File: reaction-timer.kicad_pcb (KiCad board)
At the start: 2 copper layers, 48 x 80 mm, 38 parts, among them IC1 4026, IC2 4026, IC3 4026, IC5 NE555P, IC6 NE555P, IC7 NE555P

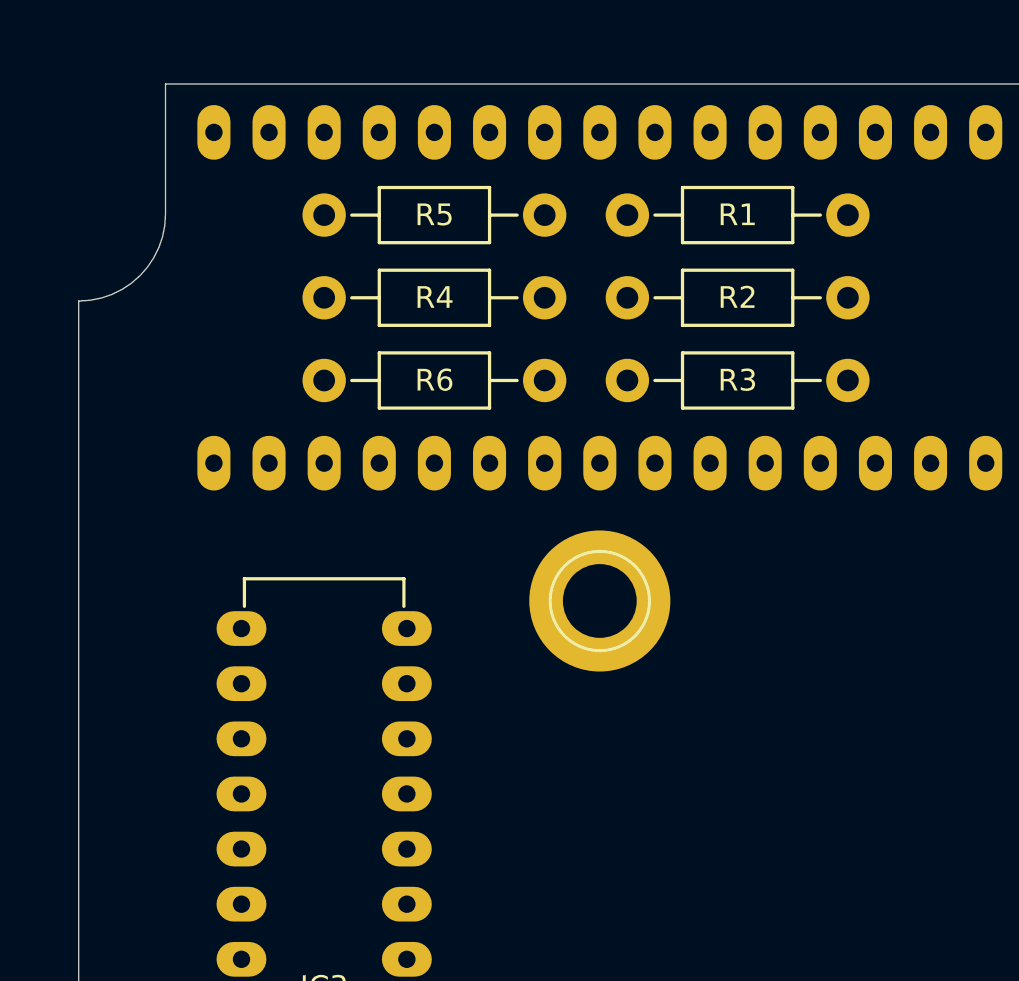
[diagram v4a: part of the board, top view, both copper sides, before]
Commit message: Start connecting some ICs on the PCB to see if it's feasible
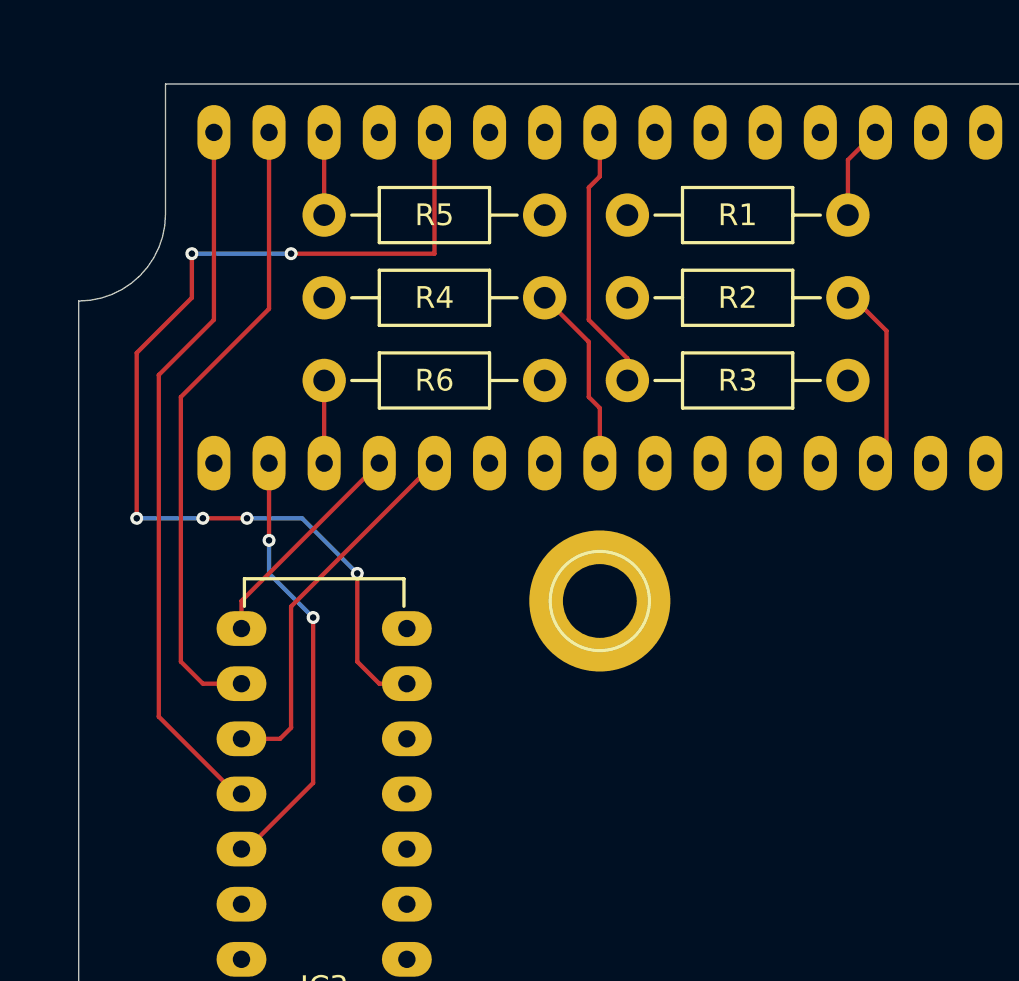
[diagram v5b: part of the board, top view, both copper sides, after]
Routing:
- net /G3: track 0.00 -> 48.0 mm, vias 0 -> 6
- net /B3: track 0.00 -> 33.3 mm
- net /A3: track 0.00 -> 29.3 mm
- net /C3: track 0.00 -> 20.1 mm, vias 0 -> 2
- net /E3: track 0.00 -> 17.4 mm
- net Net-(AFF2-Pad8): track 0.00 -> 12.4 mm
- net /D3: track 0.00 -> 10.3 mm
- net Net-(AFF1-Pad3): track 0.00 -> 8.72 mm
- net Net-(AFF2-Pad3): track 0.00 -> 8.67 mm
- net Net-(AFF1-Pad8): track 0.00 -> 4.34 mm
- net Net-(AFF3-Pad8): track 0.00 -> 3.81 mm
- net Net-(AFF3-Pad3): track 0.00 -> 3.81 mm
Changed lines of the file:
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@@
   (general
     (links 104)
-    (no_connects 104)
+    (no_connects 92)
     (area 17.504999 19.175 204.617501 195.285)
     (thickness 1.6)
     (drawings 8)
-    (tracks 0)
+    (tracks 60)
     (zones 0)
     (modules 38)
@@
   (gr_line (start 101.27 61.27) (end 101.27 67.27) (angle 90) (layer Edge.Cuts) (width 0.001))
   (gr_line (start 61.27 61.27) (end 101.27 61.27) (angle 90) (layer Edge.Cuts) (width 0.001))
+  (segment (start 92.71 71.12) (end 92.964 71.12) (width 0.2) (layer F.Cu) (net 3) (status C00000))
+  (segment (start 92.964 71.12) (end 94.488 72.644) (width 0.2) (layer F.Cu) (net 3) (status 400000))
+  (segment (start 94.488 72.644) (end 94.488 78.232) (width 0.2) (layer F.Cu) (net 3) (status 800000))
+  (segment (start 94.488 78.232) (end 93.98 78.74) (width 0.2) (layer F.Cu) (net 3) (status C00000))
+  (segment (start 92.71 67.31) (end 92.71 64.77) (width 0.2) (layer F.Cu) (net 8) (status 400000))
+  (segment (start 92.71 64.77) (end 93.98 63.5) (width 0.2) (layer F.Cu) (net 8) (status 800000))
+  (segment (start 81.28 78.74) (end 81.28 76.2) (width 0.2) (layer F.Cu) (net 13) (status 400000))
+  (segment (start 80.772 73.152) (end 78.74 71.12) (width 0.2) (layer F.Cu) (net 13) (status 800000))
+  (segment (start 80.772 75.692) (end 80.772 73.152) (width 0.2) (layer F.Cu) (net 13))
+  (segment (start 81.28 76.2) (end 80.772 75.692) (width 0.2) (layer F.Cu) (net 13))
+  (segment (start 81.28 63.5) (end 81.28 65.532) (width 0.2) (layer F.Cu) (net 18) (status 400000))
+  (segment (start 82.55 73.914) (end 82.55 74.93) (width 0.2) (layer F.Cu) (net 18) (status 800000))
+  (segment (start 80.772 72.136) (end 82.55 73.914) (width 0.2) (layer F.Cu) (net 18))
+  (segment (start 80.772 66.04) (end 80.772 72.136) (width 0.2) (layer F.Cu) (net 18))
+  (segment (start 81.28 65.532) (end 80.772 66.04) (width 0.2) (layer F.Cu) (net 18))
+  (segment (start 64.77 91.44) (end 66.548 91.44) (width 0.2) (layer F.Cu) (net 21) (status 400000))
+  (segment (start 67.056 85.344) (end 73.66 78.74) (width 0.2) (layer F.Cu) (net 21) (status 800000))
+  (segment (start 67.056 90.932) (end 67.056 85.344) (width 0.2) (layer F.Cu) (net 21))
+  (segment (start 66.548 91.44) (end 67.056 90.932) (width 0.2) (layer F.Cu) (net 21))
+  (segment (start 64.77 86.36) (end 64.77 85.09) (width 0.2) (layer F.Cu) (net 22) (status 400000))
+  (segment (start 64.77 85.09) (end 71.12 78.74) (width 0.2) (layer F.Cu) (net 22) (status 800000))
+  (segment (start 68.58 78.74) (end 68.58 74.93) (width 0.2) (layer F.Cu) (net 23) (status C00000))
+  (segment (start 64.77 96.52) (end 65.024 96.52) (width 0.2) (layer F.Cu) (net 24) (status C00000))
+  (segment (start 65.024 96.52) (end 68.072 93.472) (width 0.2) (layer F.Cu) (net 24) (status 400000))
+  (segment (start 68.072 93.472) (end 68.072 85.852) (width 0.2) (layer F.Cu) (net 24))
+  (via (at 68.072 85.852) (size 0.6) (layers F.Cu B.Cu) (net 24))
+  (segment (start 68.072 85.852) (end 66.04 83.82) (width 0.2) (layer B.Cu) (net 24))
+  (segment (start 66.04 83.82) (end 66.04 82.296) (width 0.2) (layer B.Cu) (net 24))
+  (via (at 66.04 82.296) (size 0.6) (layers F.Cu B.Cu) (net 24))
+  (segment (start 66.04 82.296) (end 66.04 78.74) (width 0.2) (layer F.Cu) (net 24) (status 800000))
+  (segment (start 64.77 93.98) (end 64.516 93.98) (width 0.2) (layer F.Cu) (net 26) (status C00000))
+  (segment (start 64.516 93.98) (end 60.96 90.424) (width 0.2) (layer F.Cu) (net 26) (status 400000))
+  (segment (start 60.96 90.424) (end 60.96 74.676) (width 0.2) (layer F.Cu) (net 26))
+  (segment (start 60.96 74.676) (end 63.5 72.136) (width 0.2) (layer F.Cu) (net 26))
+  (segment (start 63.5 72.136) (end 63.5 63.5) (width 0.2) (layer F.Cu) (net 26) (status 800000))
+  (segment (start 64.77 88.9) (end 62.992 88.9) (width 0.2) (layer F.Cu) (net 27) (status 400000))
+  (segment (start 66.04 71.628) (end 66.04 63.5) (width 0.2) (layer F.Cu) (net 27) (status 800000))
+  (segment (start 61.976 75.692) (end 66.04 71.628) (width 0.2) (layer F.Cu) (net 27))
+  (segment (start 61.976 87.884) (end 61.976 75.692) (width 0.2) (layer F.Cu) (net 27))
+  (segment (start 62.992 88.9) (end 61.976 87.884) (width 0.2) (layer F.Cu) (net 27))
+  (segment (start 68.58 67.31) (end 68.58 63.5) (width 0.2) (layer F.Cu) (net 28) (status C00000))
+  (segment (start 72.39 88.9) (end 71.12 88.9) (width 0.2) (layer F.Cu) (net 30) (status 400000))
+  (segment (start 73.66 69.088) (end 73.66 63.5) (width 0.2) (layer F.Cu) (net 30) (status 800000))
+  (segment (start 67.056 69.088) (end 73.66 69.088) (width 0.2) (layer F.Cu) (net 30))
+  (via (at 67.056 69.088) (size 0.6) (layers F.Cu B.Cu) (net 30))
+  (segment (start 62.484 69.088) (end 67.056 69.088) (width 0.2) (layer B.Cu) (net 30))
+  (via (at 62.484 69.088) (size 0.6) (layers F.Cu B.Cu) (net 30))
+  (segment (start 62.484 71.12) (end 62.484 69.088) (width 0.2) (layer F.Cu) (net 30))
+  (segment (start 59.944 73.66) (end 62.484 71.12) (width 0.2) (layer F.Cu) (net 30))
+  (segment (start 59.944 81.28) (end 59.944 73.66) (width 0.2) (layer F.Cu) (net 30))
+  (via (at 59.944 81.28) (size 0.6) (layers F.Cu B.Cu) (net 30))
+  (segment (start 62.992 81.28) (end 59.944 81.28) (width 0.2) (layer B.Cu) (net 30))
+  (via (at 62.992 81.28) (size 0.6) (layers F.Cu B.Cu) (net 30))
+  (segment (start 65.024 81.28) (end 62.992 81.28) (width 0.2) (layer F.Cu) (net 30))
+  (via (at 65.024 81.28) (size 0.6) (layers F.Cu B.Cu) (net 30))
+  (segment (start 67.564 81.28) (end 65.024 81.28) (width 0.2) (layer B.Cu) (net 30))
+  (segment (start 70.104 83.82) (end 67.564 81.28) (width 0.2) (layer B.Cu) (net 30))
+  (via (at 70.104 83.82) (size 0.6) (layers F.Cu B.Cu) (net 30))
+  (segment (start 70.104 87.884) (end 70.104 83.82) (width 0.2) (layer F.Cu) (net 30))
+  (segment (start 71.12 88.9) (end 70.104 87.884) (width 0.2) (layer F.Cu) (net 30))
 )

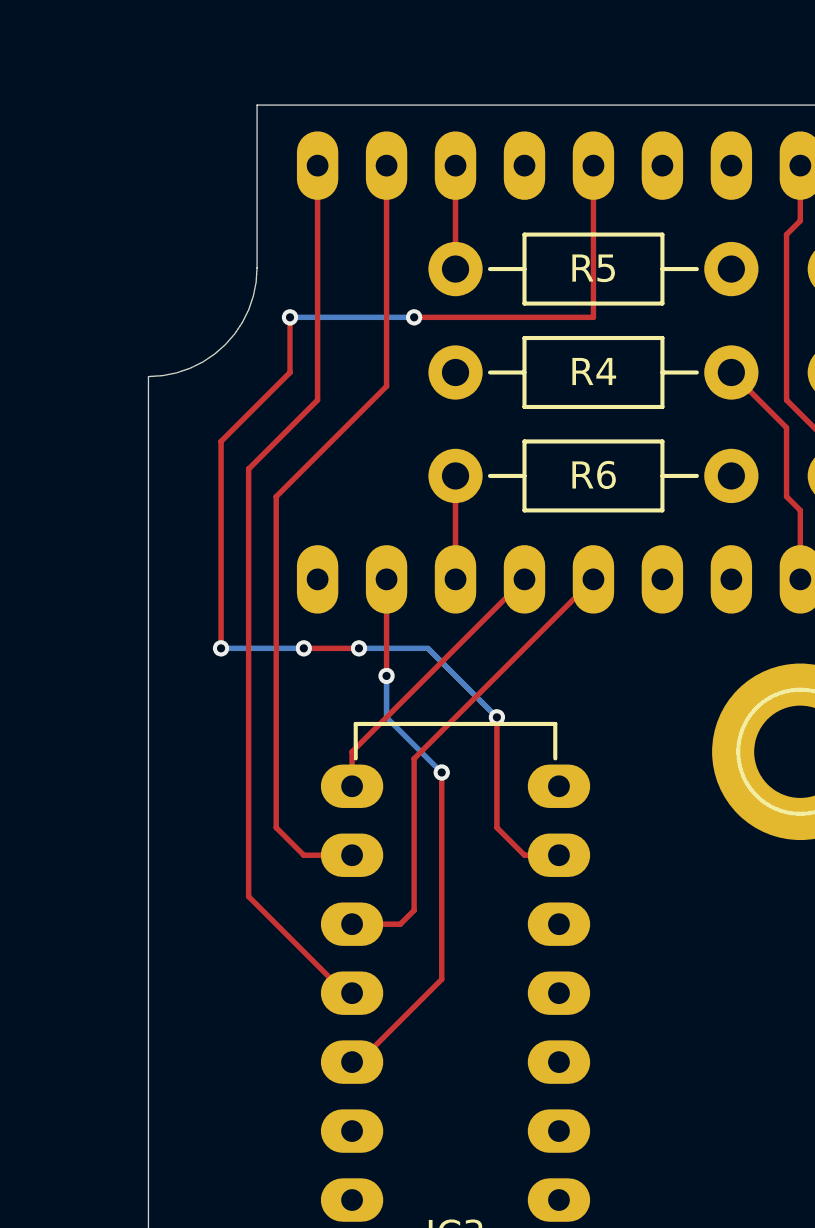
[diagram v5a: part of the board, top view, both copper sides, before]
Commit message: Connect all display pins of IC3
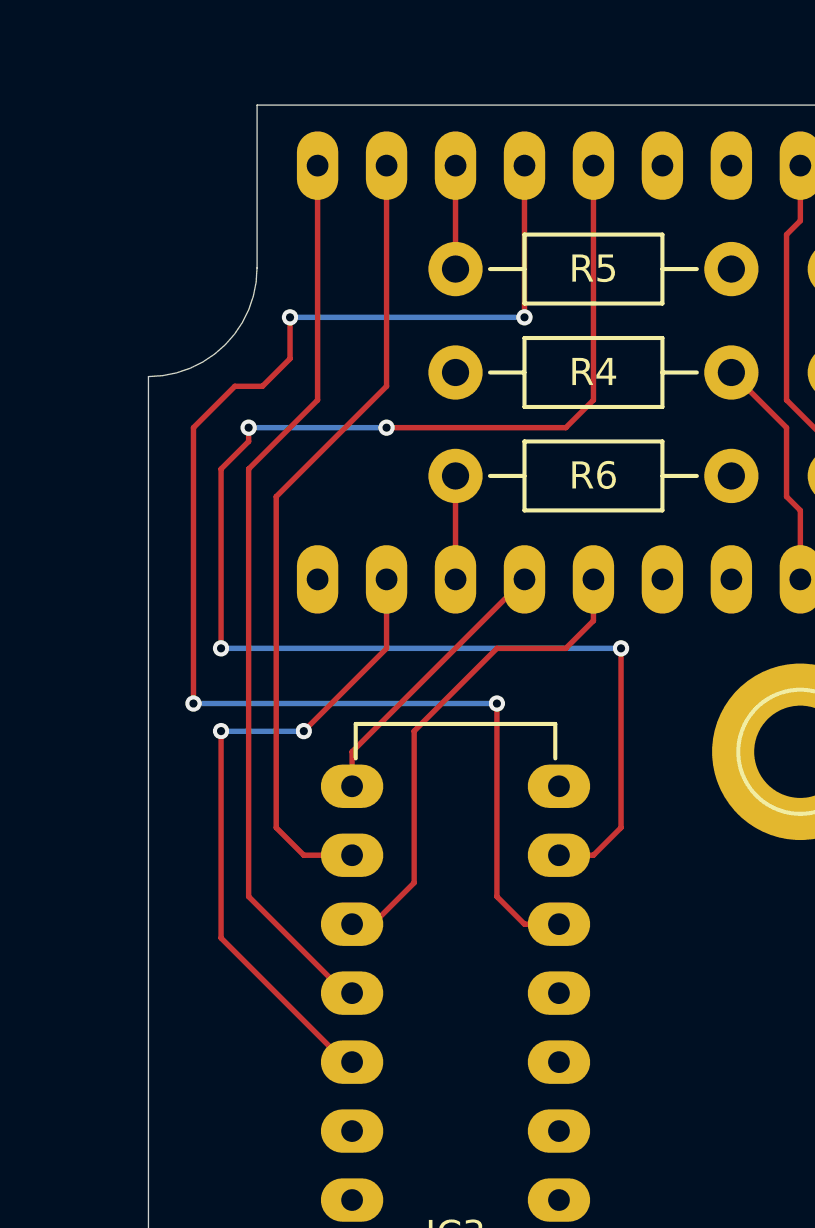
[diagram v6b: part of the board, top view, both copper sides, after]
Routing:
- net /F3: track 0.00 -> 51.5 mm, vias 0 -> 4
- net /G3: track 48.0 -> 54.3 mm, vias 6 -> 4
- net /C3: track 20.1 -> 24.2 mm
- net /E3: track 17.4 -> 18.3 mm

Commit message: Place and connect IC2
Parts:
- moved IC2 76.3 mm to (84.8, 109.2), turned to 180 degrees
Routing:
- net /F2: track 0.00 -> 41.3 mm, vias 0 -> 2
- net /B2: track 0.00 -> 38.6 mm
- net /C2: track 0.00 -> 38.3 mm, vias 0 -> 1
- net /G2: track 0.00 -> 36.4 mm
- net /A2: track 0.00 -> 32.9 mm
- net /E2: track 0.00 -> 24.2 mm
- net /D2: track 0.00 -> 17.2 mm
- net Net-(IC1-Pad15): track 0.00 -> 14.6 mm
- net Net-(IC2-Pad5): track 0.00 -> 14.6 mm

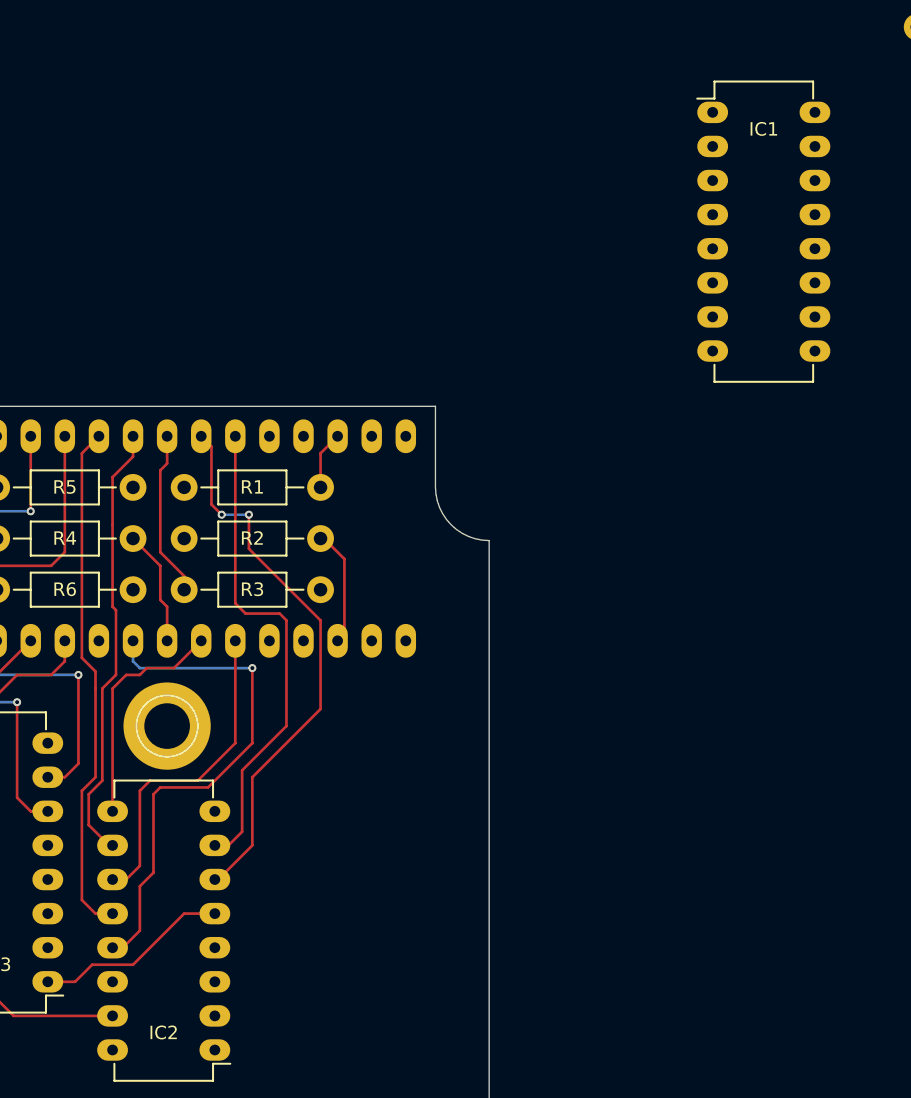
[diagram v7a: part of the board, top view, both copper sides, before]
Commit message: Place and connect IC1
- Now all 7-seg displays are connected
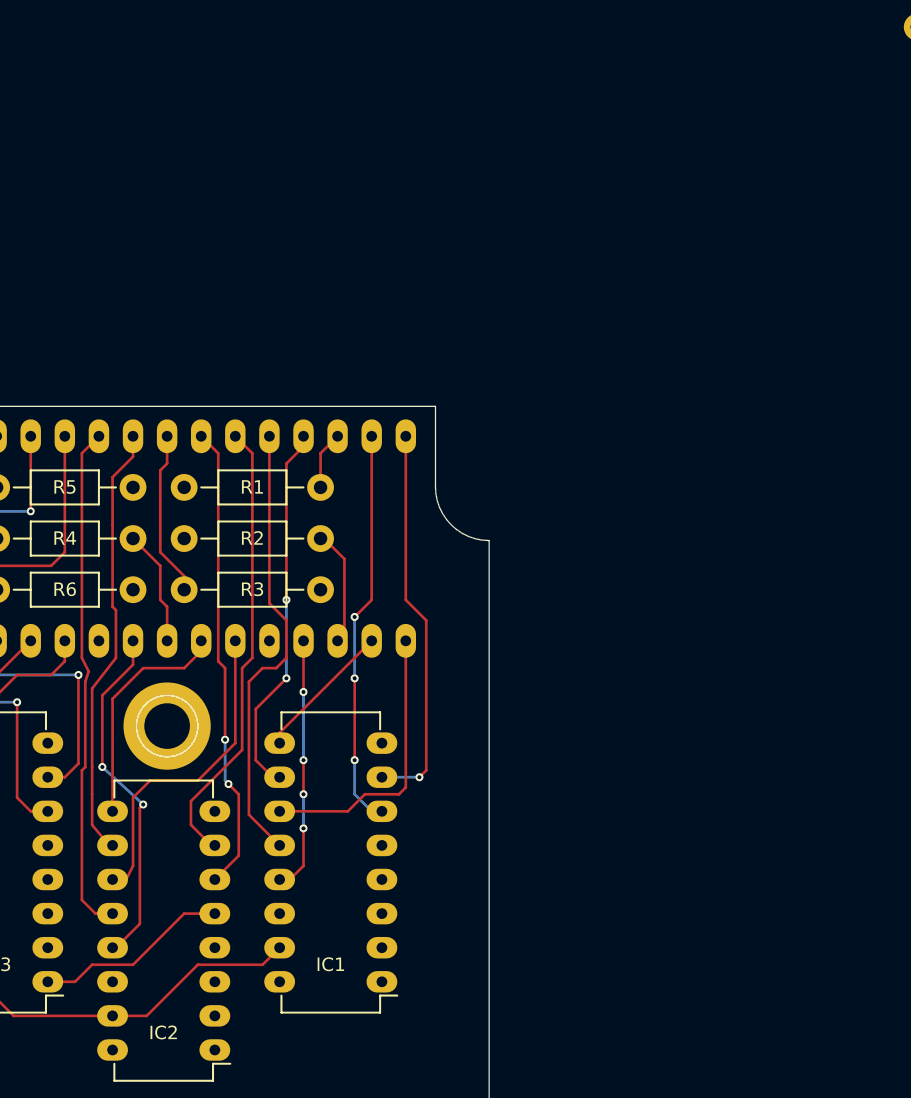
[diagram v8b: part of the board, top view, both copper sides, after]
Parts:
- moved IC1 69.3 mm to (97.3, 104.1), turned to 180 degrees
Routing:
- net /B1: track 0.00 -> 33.7 mm
- net /F1: track 0.00 -> 29.8 mm, vias 0 -> 3
- net /G1: track 0.00 -> 29.0 mm, vias 0 -> 1
- net /A1: track 0.00 -> 27.9 mm, vias 0 -> 2
- net /E1: track 0.00 -> 21.1 mm
- net /C1: track 0.00 -> 19.0 mm, vias 0 -> 4
- net Net-(IC1-Pad15): track 14.6 -> 29.1 mm
- net /C2: track 38.3 -> 26.2 mm, vias 1 -> 2
- net /D1: track 0.00 -> 10.5 mm
- net /F2: track 41.3 -> 34.9 mm
- net /G2: track 36.4 -> 33.8 mm
- net /B2: track 38.6 -> 38.0 mm
